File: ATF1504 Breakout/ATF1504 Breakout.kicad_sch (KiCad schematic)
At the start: 12 parts, among them J1 Conn_01x20_Pin, J2 Conn_01x20_Pin, J3 Conn_01x02_Pin, P1 HDR-IDC-2.54-2X5P, U1 ATF1504ASV-xAx44, U2 TLV1117LV33DCYR

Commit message: route tracks and add graphics
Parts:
- removed C1, C2: C_Polarized, easyeda2kicad:CAP-SMD_BD4.0-L4.3-W4.3-FD, symbol Device:C_Polarized
- added C1, C2: 1u, easyeda2kicad:C0603, symbol Device:C
- added C3: 0.01u, easyeda2kicad:C0603, symbol Device:C
- added R1: 0, easyeda2kicad:R0805, symbol Device:R
- added U3: DSC1001CI4-002.0480T, easyeda2kicad:OSC-SMD_4P-L3.2-W2.5-BL_1C210000BB0F, symbol easyeda2kicad:DSC1001CI4-002.0480T
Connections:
- net +3.3V: now also C1.1, C3.1, U3.4 (VDD)
- net GND: now also C1.2, C2.2, C3.2, R1.2, U3.2 (GND)
- net VCC: now also C2.1
- new net: R1.1, U3.1 (~{Standby})
- new net XCLK1: U3.3 (Output)
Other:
- note added: "External Clock 1 2.048MHz"
- moved on the sheet: U2

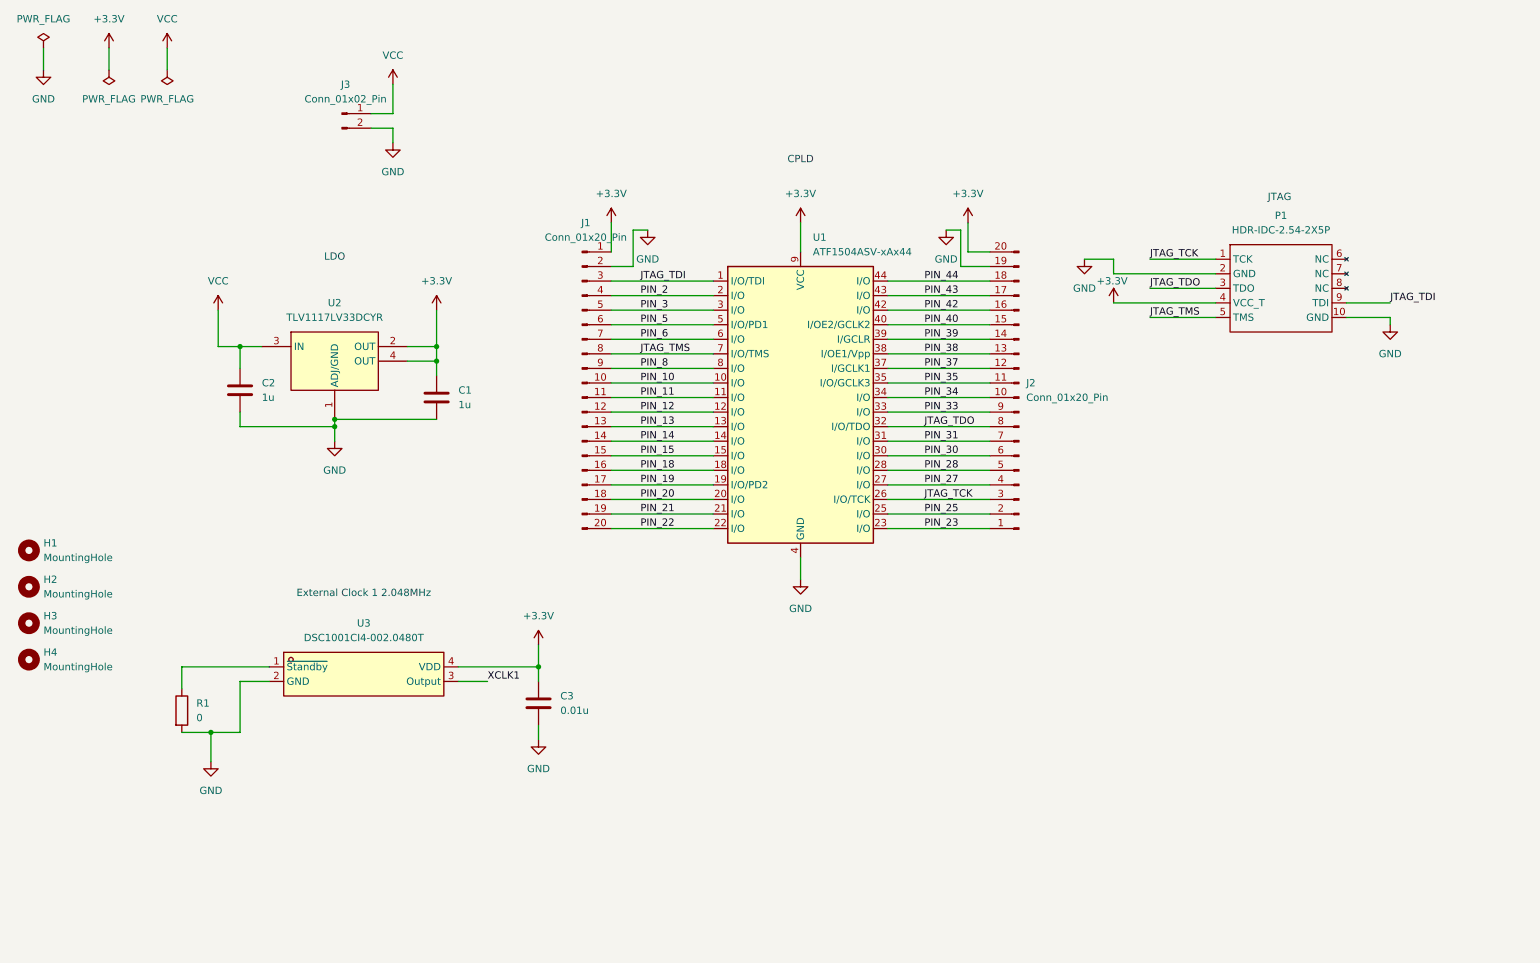
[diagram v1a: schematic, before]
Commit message: add power-on-reset and switch and led peripherals
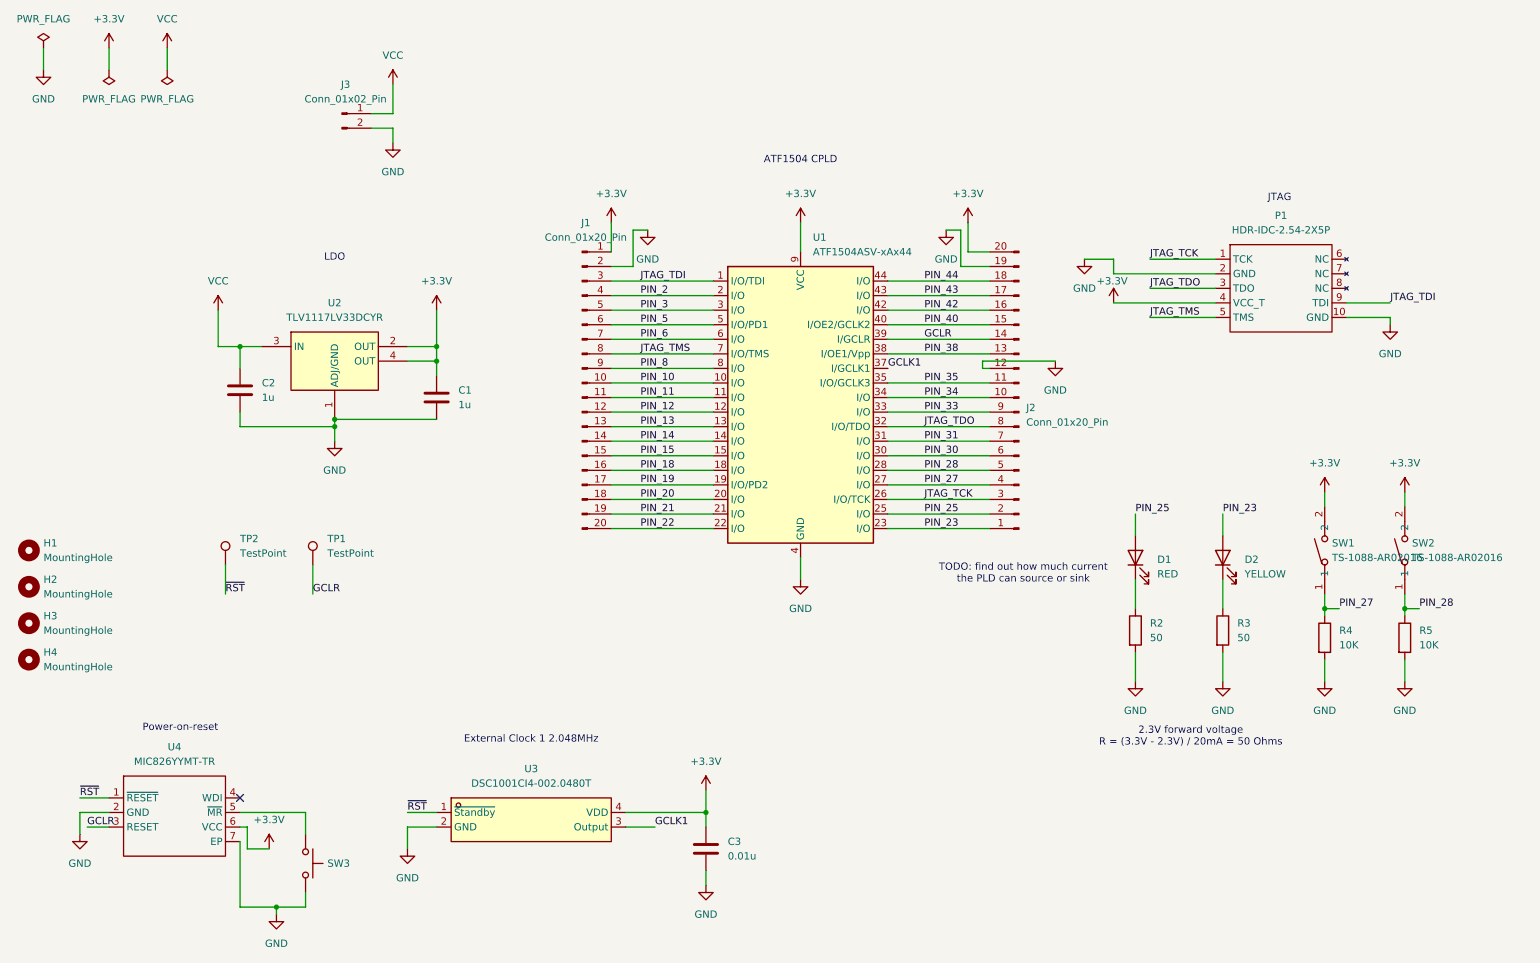
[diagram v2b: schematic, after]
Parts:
- removed R1: 0, easyeda2kicad:R0805, symbol Device:R
- added D1: RED, easyeda2kicad:LED0603-RD_RED, symbol Device:LED
- added D2: YELLOW, easyeda2kicad:LED0603-RD-YELLOW, symbol Device:LED
- added R2, R3: 50, easyeda2kicad:R0603, symbol Device:R
- added R4, R5: 10K, easyeda2kicad:R0603, symbol Device:R
- added SW1, SW2: TS-1088-AR02016, easyeda2kicad:SW-SMD_L3.9-W3.0-P4.45, symbol easyeda2kicad:TS-1088-AR02016
- added SW3: TS-1088-AR02016, easyeda2kicad:SW-SMD_L3.9-W3.0-P4.45, symbol Switch:SW_Push
- added TP1, TP2: TestPoint, TestPoint:TestPoint_THTPad_1.0x1.0mm_Drill0.5mm, symbol Connector:TestPoint
- added U4: MIC826YYMT-TR, easyeda2kicad:TDFN-6_L2.0-W2.0-P0.65-TL-EP, symbol ATF1504:MIC826
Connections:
- net XCLK1 is gone; now on net GCLK1: U3.3 (Output)
- net +3.3V: now also SW1.2, SW2.2, U4.6 (VCC)
- net GND: now also J2.12 (Pin_12), R2.2, R3.2, R4.2, R5.2, SW3.2, U4.2 (GND), U4.7 (EP)
- net PIN_23: now also D2.2 (A)
- net PIN_25: now also D1.2 (A)
- net PIN_27: now also R4.1, SW1.1
- net PIN_28: now also R5.1, SW2.1
- net ~{RST}: now reaches U3.1 (~{Standby})
- net ~{RST}: now also TP2.1, U4.1 (~{RESET})
- net PIN_37 renamed GCLK1
- net GCLK1: no longer J2.12 (Pin_12)
- net PIN_39 renamed GCLR
- net GCLR: now also TP1.1, U4.3 (RESET)
- new net: D1.1 (K), R2.1
- new net: D2.1 (K), R3.1
- new net: SW3.1, U4.5 (~{MR})
- no-connect marks 0 -> 1
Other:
- note added: "2.3V forward voltage R = (3.3V - 2.3V) / 20mA = 50 Ohms"
- note added: "ATF1504 CPLD"
- note added: "Power-on-reset"
- note added: "TODO: find out how much current the PLD can source or sink"
- note removed: "CPLD"
- moved on the sheet: C3, U3
